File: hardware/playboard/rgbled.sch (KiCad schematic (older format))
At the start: 4 parts

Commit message: Worked some more on the playboard
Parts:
- gave numbers to parts that had none: 4
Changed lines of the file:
@@
-EESchema Schematic File Version 2  date Sat 08 Jun 2013 01:37:28 AM CEST
+EESchema Schematic File Version 2
 LIBS:power
 LIBS:device
@@
 LIBS:usb_micro-b
 LIBS:microphone
+LIBS:crf
 LIBS:playboard1-cache
 EELAYER 27 0
@@
 Sheet 5 7
 Title ""
-Date "7 jun 2013"
+Date "16 jun 2013"
 Rev ""
 Comp ""
@@
 $EndDescr
 $Comp
-L PLCC6XRGBCT U?
+L PLCC6XRGBCT U4
 U 1 1 51B29101
 P 4350 3200
-F 0 "U?" H 4350 3650 60  0000 C CNN
+AR Path="/51B29079/51B29101" Ref="U4"  Part="1"
+AR Path="/51B29C83/51B29101" Ref="U5"  Part="1"
+AR Path="/51B2A046/51B29101" Ref="U6"  Part="1"
+F 0 "U6" H 4350 3650 60  0000 C CNN
 F 1 "PLCC6XRGBCT" H 4350 2700 60  0000 C CNN
 F 2 "" H 4350 3200 60  0000 C CNN
@@
 $EndComp
 $Comp
-L R R?
+L R R28
 U 1 1 51B29110
 P 3750 2900
-F 0 "R?" V 3830 2900 40  0000 C CNN
+AR Path="/51B29079/51B29110" Ref="R28"  Part="1"
+AR Path="/51B29C83/51B29110" Ref="R31"  Part="1"
+AR Path="/51B2A046/51B29110" Ref="R34"  Part="1"
+F 0 "R34" V 3830 2900 40  0000 C CNN
 F 1 "R" V 3757 2901 40  0000 C CNN
 F 2 "~" V 3680 2900 30  0000 C CNN
@@
 $EndComp
 $Comp
-L R R?
+L R R29
 U 1 1 51B29140
 P 3750 3150
-F 0 "R?" V 3830 3150 40  0000 C CNN
+AR Path="/51B29079/51B29140" Ref="R29"  Part="1"
+AR Path="/51B29C83/51B29140" Ref="R32"  Part="1"
+AR Path="/51B2A046/51B29140" Ref="R35"  Part="1"
+F 0 "R35" V 3830 3150 40  0000 C CNN
 F 1 "R" V 3757 3151 40  0000 C CNN
 F 2 "~" V 3680 3150 30  0000 C CNN
@@
 $EndComp
 $Comp
-L R R?
+L R R30
 U 1 1 51B29146
 P 3750 3400
-F 0 "R?" V 3830 3400 40  0000 C CNN
+AR Path="/51B29079/51B29146" Ref="R30"  Part="1"
+AR Path="/51B29C83/51B29146" Ref="R33"  Part="1"
+AR Path="/51B2A046/51B29146" Ref="R36"  Part="1"
+F 0 "R36" V 3830 3400 40  0000 C CNN
 F 1 "R" V 3757 3401 40  0000 C CNN
 F 2 "~" V 3680 3400 30  0000 C CNN

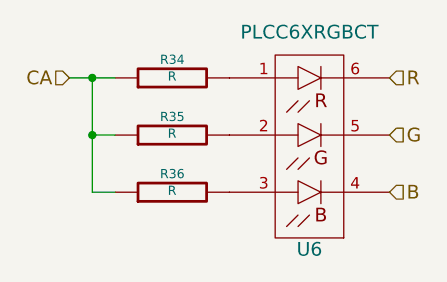
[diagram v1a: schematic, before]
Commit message: Redesigned board for playboard.
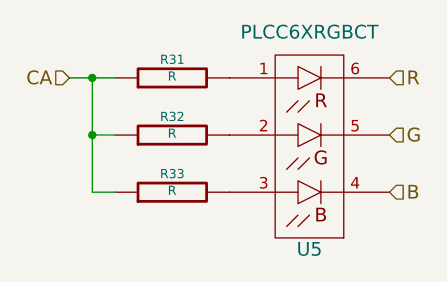
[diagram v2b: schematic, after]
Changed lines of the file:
@@
 AR Path="/51B29C83/51B29101" Ref="U5"  Part="1"
 AR Path="/51B2A046/51B29101" Ref="U6"  Part="1"
-F 0 "U6" H 4350 3650 60  0000 C CNN
+F 0 "U5" H 4350 3650 60  0000 C CNN
 F 1 "PLCC6XRGBCT" H 4350 2700 60  0000 C CNN
 F 2 "" H 4350 3200 60  0000 C CNN
@@
 AR Path="/51B29C83/51B29110" Ref="R31"  Part="1"
 AR Path="/51B2A046/51B29110" Ref="R34"  Part="1"
-F 0 "R34" V 3830 2900 40  0000 C CNN
+F 0 "R31" V 3830 2900 40  0000 C CNN
 F 1 "R" V 3757 2901 40  0000 C CNN
 F 2 "~" V 3680 2900 30  0000 C CNN
@@
 AR Path="/51B29C83/51B29140" Ref="R32"  Part="1"
 AR Path="/51B2A046/51B29140" Ref="R35"  Part="1"
-F 0 "R35" V 3830 3150 40  0000 C CNN
+F 0 "R32" V 3830 3150 40  0000 C CNN
 F 1 "R" V 3757 3151 40  0000 C CNN
 F 2 "~" V 3680 3150 30  0000 C CNN
@@
 AR Path="/51B29C83/51B29146" Ref="R33"  Part="1"
 AR Path="/51B2A046/51B29146" Ref="R36"  Part="1"
-F 0 "R36" V 3830 3400 40  0000 C CNN
+F 0 "R33" V 3830 3400 40  0000 C CNN
 F 1 "R" V 3757 3401 40  0000 C CNN
 F 2 "~" V 3680 3400 30  0000 C CNN
